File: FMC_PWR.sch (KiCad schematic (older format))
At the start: 75 parts, among them IC1 INA226AIDGSR, Q1 FDPC8011S, Q2 MMBT3904T-7-F, U1 MPM3840GQV-Z, U2 MAX15301AA02+CJK

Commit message: Update May --> See Update Note
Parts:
- added NT2, NT3: Net-Tie_2, ApotheoTech_CXP_Lib:Short_0201, symbol Device:Net-Tie_2
- C25, C29: URL https://www.digikey.com/en/products/detail/tdk-corporation/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 -> https://www.digikey.com/en/products/detail/C1005X5R1E105K05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
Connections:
- net UTIL_3V3 is gone; now on net FMC_3V3: C21.1, IC1.6 (VS), R13.1, R23.1, R27.1, R28.2, R29.1
- net DCR_P: now also NT3.1, NT3.2
- net VADJ_FMC_BUS: now also NT2.1, NT2.2
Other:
- moved on the sheet: R18
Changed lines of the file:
@@
 Wire Wire Line
 	4200 4400 4500 4400
-Connection ~ 4500 4100
 Wire Wire Line
 	5350 4000 5450 4000
@@
 	5450 4050 5450 4000
 Connection ~ 5450 4000
-Wire Wire Line
-	4500 4400 5900 4400
 Connection ~ 4500 4400
 Wire Wire Line
@@
 L Device:R R?
 U 1 1 63BE0921
-P 6050 4400
+P 6900 4400
 AR Path="/6314CDE6/63BE0921" Ref="R?"  Part="1"
 AR Path="/62011758/63BE0921" Ref="R18"  Part="1"
-F 0 "R18" V 6085 4555 50  0000 L CNN
-F 1 "1.69k" V 6095 4065 50  0000 L CNN
-F 2 "Resistor_SMD:R_0402_1005Metric" V 5980 4400 50  0001 C CNN
-F 3 "~" H 6050 4400 50  0001 C CNN
-F 4 "ERJ-2RKF1691X " H 6050 4400 50  0001 C CNN "PartNumber"
-F 5 "1%" H 6050 4400 50  0001 C CNN "Tol"
-F 6 "1/10W" H 6050 4400 50  0001 C CNN "Power"
-	1    6050 4400
+F 0 "R18" V 6935 4555 50  0000 L CNN
+F 1 "1.69k" V 6945 4065 50  0000 L CNN
+F 2 "Resistor_SMD:R_0402_1005Metric" V 6830 4400 50  0001 C CNN
+F 3 "~" H 6900 4400 50  0001 C CNN
+F 4 "ERJ-2RKF1691X " H 6900 4400 50  0001 C CNN "PartNumber"
+F 5 "1%" H 6900 4400 50  0001 C CNN "Tol"
+F 6 "1/10W" H 6900 4400 50  0001 C CNN "Power"
+	1    6900 4400
 	0    -1   -1   0
 $EndComp
 Text Label 10000 4400 2    50   ~ 0
 VADJ_FMC_FET_SWITCH
-Text Label 10000 4100 2    50   ~ 0
+Text Label 9800 4100 2    50   ~ 0
 VADJ_FMC_BUS
 Text Notes 8795 4555 0    50   ~ 0
@@
 Wire Wire Line
 	2400 4250 2400 4200
-Text GLabel 2200 4200 0    50   Output ~ 0
-UTIL_3V3
 Text HLabel 2200 3900 0    50   Output ~ 0
 VADJ_ALERT
@@
 Connection ~ 950  7150
 Wire Wire Line
-	6200 4400 10000 4400
-Wire Wire Line
-	4500 4100 10000 4100
-Wire Wire Line
 	4900 3900 9500 3900
 Wire Wire Line
@@
 	0    -1   -1   0
 $EndComp
-Text GLabel 2200 3750 0    50   Output ~ 0
-UTIL_3V3
 Wire Wire Line
 	2200 3900 2800 3900
@@
 	8200 2000 8450 2000
 Connection ~ 8200 2000
-Text GLabel 8450 2000 2    50   Output ~ 0
-UTIL_3V3
 $Comp
 L Device:R R?
@@
 Wire Wire Line
 	6500 2750 6400 2750
-Text GLabel 6250 2100 0    50   Output ~ 0
-UTIL_3V3
 Wire Wire Line
 	6500 2100 6250 2100
@@
 F 6 "25V" H 12215 4230 50  0000 C CNN "Voltage"
 F 7 "X5R" H 12400 4150 50  0001 C CNN "Temp_Val"
-F 8 "https://www.digikey.com/en/products/detail/tdk-corporation/C1005X5R1E105K050BE/7907739" V 12400 4150 50  0001 C CNN "URL"
+F 8 "https://www.digikey.com/en/products/detail/C1005X5R1E105K050BE/445-175215-1-ND/7907779?itemSeq=374777296" V 12400 4150 50  0001 C CNN "URL"
 	1    12400 4150
 	-1   0    0    1
@@
 F 6 "25V" H 12665 4230 50  0000 C CNN "Voltage"
 F 7 "X5R" H 12850 4150 50  0001 C CNN "Temp_Val"
-F 8 "https://www.digikey.com/en/products/detail/tdk-corporation/C1005X5R1E105K050BE/7907739" V 12850 4150 50  0001 C CNN "URL"
+F 8 "https://www.digikey.com/en/products/detail/C1005X5R1E105K050BE/445-175215-1-ND/7907779?itemSeq=374777296" V 12850 4150 50  0001 C CNN "URL"
 	1    12850 4150
 	-1   0    0    1
@@
 Text Label 4850 4400 0    50   ~ 0
 DCR_P
+Text GLabel 6250 2100 0    50   Output ~ 0
+FMC_3V3
+Text GLabel 8450 2000 2    50   Output ~ 0
+FMC_3V3
+Text GLabel 2200 3750 0    50   Output ~ 0
+FMC_3V3
+Text GLabel 2200 4200 0    50   Output ~ 0
+FMC_3V3
+$Comp
+L Device:Net-Tie_2 NT3
+U 1 1 624F6881
+P 6200 4400
+F 0 "NT3" H 6200 4450 50  0000 C CNN
+F 1 "Net-Tie_2" H 6200 4490 50  0001 C CNN
+F 2 "ApotheoTech_CXP_Lib:Short_0201" H 6200 4400 50  0001 C CNN
+F 3 "~" H 6200 4400 50  0001 C CNN
+	1    6200 4400
+	1    0    0    -1
+$EndComp
+Wire Wire Line
+	4500 4400 6100 4400
+Wire Wire Line
+	6300 4400 6750 4400
+Wire Wire Line
+	7050 4400 10000 4400
+$Comp
+L Device:Net-Tie_2 NT2
+U 1 1 62597436
+P 6200 4100
+F 0 "NT2" H 6200 4045 50  0000 C CNN
+F 1 "Net-Tie_2" H 6200 4190 50  0001 C CNN
+F 2 "ApotheoTech_CXP_Lib:Short_0201" H 6200 4100 50  0001 C CNN
+F 3 "~" H 6200 4100 50  0001 C CNN
+	1    6200 4100
+	1    0    0    -1
+$EndComp
+Wire Wire Line
+	4500 4100 6100 4100
+Connection ~ 4500 4100
+Wire Wire Line
+	6300 4100 10000 4100
+Text Label 6375 4100 0    50   ~ 0
+DCR_N
+Text Label 6350 4400 0    50   ~ 0
+DCR_P
 $EndSCHEMATC

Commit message: Pre-Production Push
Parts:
- added R50: 10K, Resistor_SMD:R_0402_1005Metric, symbol Device:R
- C8: value 2200pF -> 0.22uF; PartNumber GRM155R71H222JA01J -> C1005X5R1E224K050BC; Temp_Val X7R -> X5R; Tolerance +-5% -> +-10%; Voltage 50V -> 25V
- L2: footprint Inductor_SMD:L_Wuerth_HCI-5040 -> ApotheoTech_CXP_Lib:744316047
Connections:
- net 12V_IN: no longer C16.2, C17.2, Q1.8 (V+), Q1.9 (V+)
- net FMC_12V: now also C16.2, C17.2, Q1.8 (V+), Q1.9 (V+)
- net VCCOEN_PL_M2C: no longer U2.12 (EN)
- net INA226_ALERT renamed HDC19_INA226_ALERT
- net VADJ_ALERT renamed HDC20_VADJ_ALERT
- new net UTIL_3V3: R50.1
- new net VADJ_EN: R50.2, U2.12 (EN)
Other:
- note added: "Note, 4V maximum for this pin,\nVCCOEN is 5V. Use a PIC signal for EN"
- note added: "Page 73/95 ZCU106 Schematic for Reference"
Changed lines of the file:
@@
 $Descr A3 16535 11693
 encoding utf-8
-Sheet 17 20
+Sheet 16 20
 Title "FMC Power (VADJ, 3.3V, and 12V filt)"
 Date "2022-01-04"
@@
 	1    0    0    -1
 $EndComp
-Text GLabel 6400 4550 0    50   Output ~ 0
-12V_IN
 Wire Wire Line
 	6400 4550 6500 4550
@@
 	4900 6000 4900 5950
 Text HLabel 2200 5250 0    50   Input ~ 0
-VCCOEN_PL_M2C
+VADJ_EN
 $Comp
 L Device:C C?
@@
 AR Path="/62011758/63CD5630" Ref="C8"  Part="1"
 F 0 "C8" H 4140 5310 50  0000 C CNN
-F 1 "2200pF" H 4055 5380 50  0000 C CNN
+F 1 "0.22uF" H 4055 5380 50  0000 C CNN
 F 2 "Capacitor_SMD:C_0402_1005Metric" H 4338 5200 50  0001 C CNN
 F 3 "~" H 4300 5350 50  0001 C CNN
-F 4 "GRM155R71H222JA01J " H 4300 5350 50  0001 C CNN "PartNumber"
-F 5 "+-5%" H 4300 5350 50  0001 C CNN "Tolerance"
-F 6 "50V" H 4115 5450 50  0000 C CNN "Voltage"
-F 7 "X7R" H 4300 5350 50  0001 C CNN "Temp_Val"
+F 4 "C1005X5R1E224K050BC " H 4300 5350 50  0001 C CNN "PartNumber"
+F 5 "+-10%" H 4300 5350 50  0001 C CNN "Tolerance"
+F 6 "25V" H 4115 5450 50  0000 C CNN "Voltage"
+F 7 "X5R" H 4300 5350 50  0001 C CNN "Temp_Val"
 	1    4300 5350
 	-1   0    0    1
@@
 F 0 "L2" V 7175 5435 50  0000 C CNN
 F 1 "470nH" V 7160 5785 50  0000 C CNN
-F 2 "Inductor_SMD:L_Wuerth_HCI-5040" H 7100 5600 50  0001 C CNN
+F 2 "ApotheoTech_CXP_Lib:744316047" H 7100 5600 50  0001 C CNN
 F 3 "~" H 7100 5600 50  0001 C CNN
 F 4 "744316047 " V 7100 5600 50  0001 C CNN "PartNumber"
@@
 	2900 4100 2200 4100
 Wire Wire Line
-	2900 5250 2200 5250
+	2900 5250 2300 5250
 Text HLabel 2200 4600 0    50   Output ~ 0
 VADJ_FMC_PG
@@
 	2400 4250 2400 4200
 Text HLabel 2200 3900 0    50   Output ~ 0
-VADJ_ALERT
+HDC20_VADJ_ALERT
 Wire Wire Line
 	2900 6950 2800 6950
@@
 Connection ~ 6650 2900
 Text HLabel 6400 2750 0    50   Output ~ 0
-INA226_ALERT
+HDC19_INA226_ALERT
 $Comp
 L Device:R R?
@@
 Text Label 6350 4400 0    50   ~ 0
 DCR_P
+Text GLabel 6400 4550 0    50   Input ~ 0
+FMC_12V
+Text Notes 3855 1695 0    50   ~ 0
+Page 73/95 ZCU106 Schematic for Reference
+Text Notes 690  4480 0    50   ~ 0
+Note, 4V maximum for this pin,\nVCCOEN is 5V. Use a PIC signal for EN
+$Comp
+L Device:R R?
+U 1 1 631E9944
+P 2300 5050
+AR Path="/5F71E87D/631E9944" Ref="R?"  Part="1"
+AR Path="/6314F1AA/631E9944" Ref="R?"  Part="1"
+AR Path="/6314F719/631E9944" Ref="R?"  Part="1"
+AR Path="/6314DEA9/631E9944" Ref="R?"  Part="1"
+AR Path="/62011758/631E9944" Ref="R50"  Part="1"
+F 0 "R50" H 2370 5141 50  0000 L CNN
+F 1 "10K" H 2370 5050 50  0000 L CNN
+F 2 "Resistor_SMD:R_0402_1005Metric" V 2230 5050 50  0001 C CNN
+F 3 "~" H 2300 5050 50  0001 C CNN
+F 4 "1%" H 2370 4959 50  0000 L CNN "Tolerance"
+F 5 "1/10W" H 2300 5050 50  0001 C CNN "Power"
+F 6 "ERJ-2RKF1002X" H 2300 5050 50  0001 C CNN "PartNumber"
+F 7 "https://www.digikey.com/en/products/detail/panasonic-electronic-components/ERJ-2RKF1002X/192073" H 2300 5050 50  0001 C CNN "URL"
+	1    2300 5050
+	1    0    0    -1
+$EndComp
+Wire Wire Line
+	2300 5200 2300 5250
+Connection ~ 2300 5250
+Wire Wire Line
+	2300 5250 2200 5250
+Text GLabel 2150 4800 0    50   Input ~ 0
+UTIL_3V3
+Wire Wire Line
+	2150 4800 2300 4800
+Wire Wire Line
+	2300 4800 2300 4900
 $EndSCHEMATC

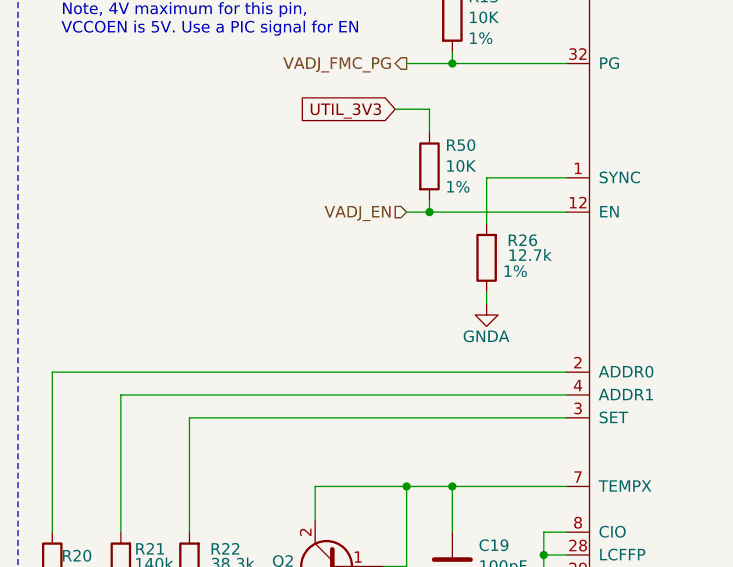
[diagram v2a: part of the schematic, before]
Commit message: Update to Kicad 7
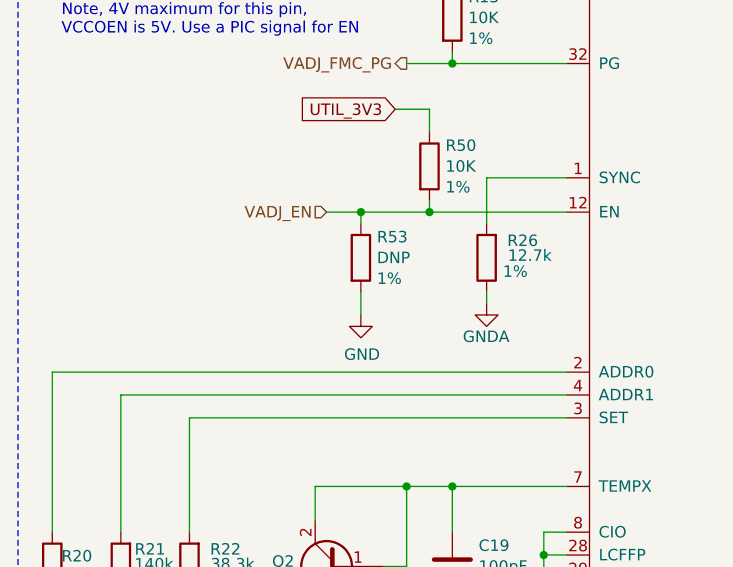
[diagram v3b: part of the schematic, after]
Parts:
- added R53: DNP, Resistor_SMD:R_0402_1005Metric, symbol Device:R
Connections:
- net GND: now also R53.2
- net VADJ_EN: now also R53.1
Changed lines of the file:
@@
 Wire Wire Line
 	4900 6000 4900 5950
-Text HLabel 2200 5250 0    50   Input ~ 0
+Text HLabel 1850 5250 0    50   Input ~ 0
 VADJ_EN
 $Comp
@@
 	2300 5200 2300 5250
 Connection ~ 2300 5250
-Wire Wire Line
-	2300 5250 2200 5250
 Text GLabel 2150 4800 0    50   Input ~ 0
 UTIL_3V3
@@
 Wire Wire Line
 	2300 4800 2300 4900
+$Comp
+L Device:R R?
+U 1 1 63AE0F0C
+P 2000 5450
+AR Path="/5F71E87D/63AE0F0C" Ref="R?"  Part="1"
+AR Path="/6314F1AA/63AE0F0C" Ref="R?"  Part="1"
+AR Path="/6314F719/63AE0F0C" Ref="R?"  Part="1"
+AR Path="/6314DEA9/63AE0F0C" Ref="R?"  Part="1"
+AR Path="/62011758/63AE0F0C" Ref="R53"  Part="1"
+F 0 "R53" H 2070 5541 50  0000 L CNN
+F 1 "DNP" H 2070 5450 50  0000 L CNN
+F 2 "Resistor_SMD:R_0402_1005Metric" V 1930 5450 50  0001 C CNN
+F 3 "~" H 2000 5450 50  0001 C CNN
+F 4 "1%" H 2070 5359 50  0000 L CNN "Tolerance"
+F 5 "1/10W" H 2000 5450 50  0001 C CNN "Power"
+F 6 "ERJ-2RKF1002X" H 2000 5450 50  0001 C CNN "PartNumber"
+F 7 "https://www.digikey.com/en/products/detail/panasonic-electronic-components/ERJ-2RKF1002X/192073" H 2000 5450 50  0001 C CNN "URL"
+	1    2000 5450
+	1    0    0    -1
+$EndComp
+Wire Wire Line
+	1850 5250 2000 5250
+Wire Wire Line
+	2000 5300 2000 5250
+Connection ~ 2000 5250
+Wire Wire Line
+	2000 5250 2300 5250
+Wire Wire Line
+	2000 5600 2000 5700
+$Comp
+L power:GND #PWR045
+U 1 1 63BA4A79
+P 2000 5700
+F 0 "#PWR045" H 2000 5450 50  0001 C CNN
+F 1 "GND" H 2005 5527 50  0000 C CNN
+F 2 "" H 2000 5700 50  0001 C CNN
+F 3 "" H 2000 5700 50  0001 C CNN
+	1    2000 5700
+	1    0    0    -1
+$EndComp
 $EndSCHEMATC
